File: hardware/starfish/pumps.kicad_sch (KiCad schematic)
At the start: 7 parts, among them J1001 Pump, Q1001 PSMN011-30YLC

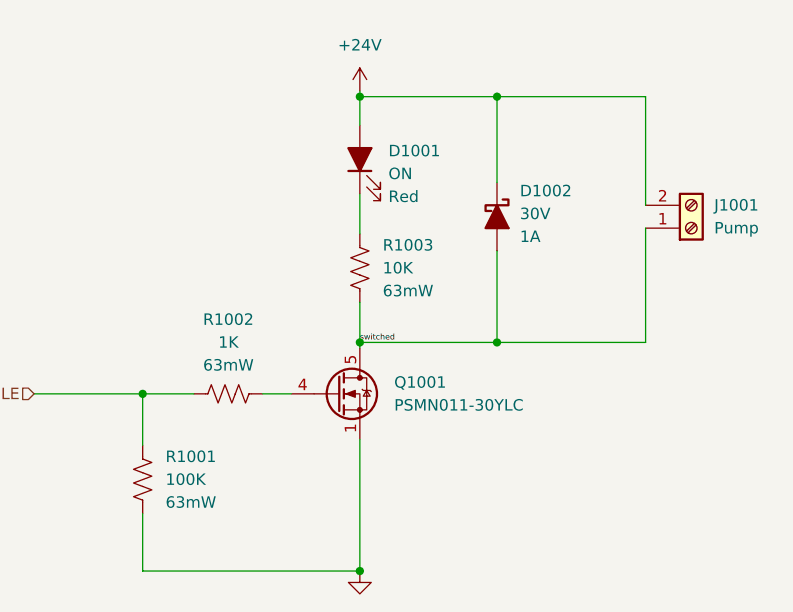
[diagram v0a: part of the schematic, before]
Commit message: Mostly finished starfish schematic, ready for layout!
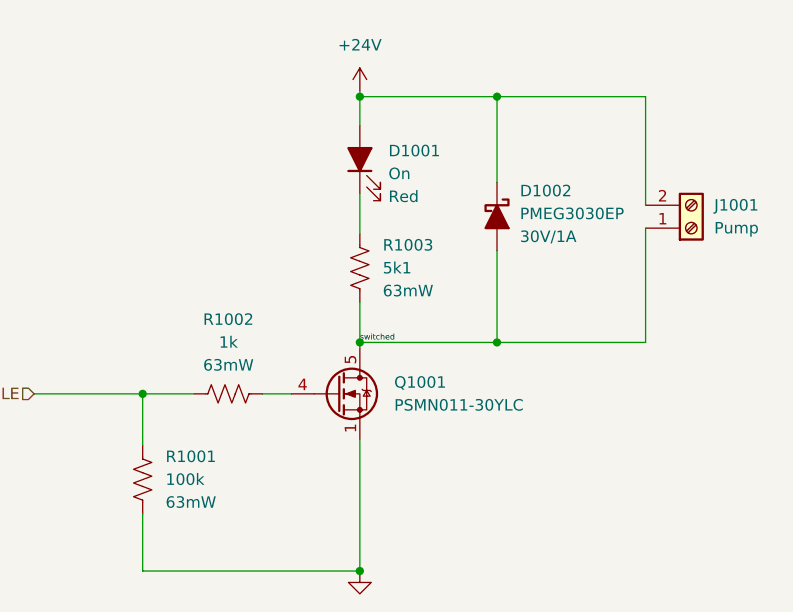
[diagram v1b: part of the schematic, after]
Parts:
- D1001: value ON -> On
- D1002: value 30V -> PMEG3030EP; Rating 1A -> 30V/1A
- Q1001: mpn (none) -> PSMN011-30YLC
- R1001: value 100K -> 100k; footprint (none) -> winterbloom:R_0402_HandSolder
- R1002: value 1K -> 1k; footprint (none) -> winterbloom:R_0402_HandSolder; mpn (none) -> RC0402JR-071KL
- R1003: value 10K -> 5k1; footprint (none) -> winterbloom:R_0402_HandSolder; mpn (none) -> AC0603FR-075K1L
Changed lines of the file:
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@@
       (effects (font (size 1.27 1.27)) (justify right))
     )
-    (property "Value" "ON" (id 1) (at 133.985 75.8824 90)
+    (property "Value" "On" (id 1) (at 133.985 75.8824 90)
       (effects (font (size 1.27 1.27)) (justify right))
     )
@@
       (effects (font (size 1.27 1.27)) (justify left))
     )
-    (property "Value" "100K" (id 1) (at 109.22 109.8549 0)
+    (property "Value" "100k" (id 1) (at 109.22 109.8549 0)
       (effects (font (size 1.27 1.27)) (justify left))
     )
-    (property "Footprint" "" (id 2) (at 107.696 110.109 90)
+    (property "Footprint" "winterbloom:R_0402_HandSolder" (id 2) (at 107.696 110.109 90)
       (effects (font (size 1.27 1.27)) hide)
     )
@@
       (effects (font (size 1.27 1.27)) (justify left))
     )
-    (property "Value" "30V" (id 1) (at 148.59 80.3274 90)
+    (property "Value" "PMEG3030EP" (id 1) (at 148.59 80.3274 90)
       (effects (font (size 1.27 1.27)) (justify left))
     )
@@
       (effects (font (size 1.27 1.27)) hide)
     )
-    (property "Rating" "1A" (id 4) (at 148.59 82.8674 90)
+    (property "Rating" "30V/1A" (id 4) (at 148.59 82.8674 90)
       (effects (font (size 1.27 1.27)) (justify left))
     )
@@
     (in_bom yes) (on_board yes) (fields_autoplaced)
     (property "Reference" "R1002" (id 0) (at 116.205 92.075 90))
-    (property "Value" "1K" (id 1) (at 116.205 94.615 90))
-    (property "Footprint" "" (id 2) (at 116.459 99.314 90)
+    (property "Value" "1k" (id 1) (at 116.205 94.615 90))
+    (property "Footprint" "winterbloom:R_0402_HandSolder" (id 2) (at 116.459 99.314 90)
       (effects (font (size 1.27 1.27)) hide)
     )
@@
     )
     (property "Rating" "63mW" (id 4) (at 116.205 97.155 90))
+    (property "mpn" "RC0402JR-071KL" (id 5) (at 116.205 100.33 0)
+      (effects (font (size 1.27 1.27)) hide)
+    )
     (pin "1")
     (pin "2")
@@
       (effects (font (size 1.27 1.27)) (justify left))
     )
-    (property "Value" "10K" (id 1) (at 133.35 86.3599 0)
+    (property "Value" "5k1" (id 1) (at 133.35 86.3599 0)
       (effects (font (size 1.27 1.27)) (justify left))
     )
-    (property "Footprint" "" (id 2) (at 131.826 86.614 90)
+    (property "Footprint" "winterbloom:R_0402_HandSolder" (id 2) (at 131.826 86.614 90)
       (effects (font (size 1.27 1.27)) hide)
     )
@@
       (effects (font (size 1.27 1.27)) hide)
     )
-    (property "mpn" "" (id 4) (at 130.81 86.36 0)
+    (property "mpn" "AC0603FR-075K1L" (id 4) (at 130.81 86.36 0)
       (effects (font (size 1.27 1.27)) hide)
     )
@@
       (effects (font (size 1.27 1.27)) hide)
     )
+    (property "mpn" "PSMN011-30YLC" (id 4) (at 128.27 100.33 0)
+      (effects (font (size 1.27 1.27)) hide)
+    )

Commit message: Layout and routing mostly done! Just gotta make it prettier!
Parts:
- D1002: footprint Diode_SMD:D_SOD-128 -> winterbloom:D_SOD-128
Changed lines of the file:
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@@
       (effects (font (size 1.27 1.27)) (justify left))
     )
-    (property "Footprint" "Diode_SMD:D_SOD-128" (id 2) (at 146.05 80.645 0)
+    (property "Footprint" "winterbloom:D_SOD-128" (id 2) (at 146.05 80.645 0)
       (effects (font (size 1.27 1.27)) hide)
     )

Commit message: Run through purchasing, update some cap sizes
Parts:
- D1002: mpn (none) -> PMEG3030EP,115
- Q1001: mpn PSMN011-30YLC -> PSMN011-30YLC, BUK9Y40-55B
- R1001: mpn (none) -> RC0402DR-07100KL
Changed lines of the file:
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@@
       (effects (font (size 1.27 1.27)) (justify left))
+    )
+    (property "mpn" "RC0402DR-07100KL" (id 5) (at 106.68 109.855 0)
+      (effects (font (size 1.27 1.27)) hide)
     )
     (pin "1")
@@
     (property "Rating" "30V/1A" (id 4) (at 148.59 82.8674 90)
       (effects (font (size 1.27 1.27)) (justify left))
+    )
+    (property "mpn" "PMEG3030EP,115" (id 5) (at 146.05 80.645 0)
+      (effects (font (size 1.27 1.27)) hide)
     )
     (pin "1")
@@
       (effects (font (size 1.27 1.27)) hide)
     )
-    (property "mpn" "PSMN011-30YLC" (id 4) (at 128.27 100.33 0)
+    (property "mpn" "PSMN011-30YLC, BUK9Y40-55B" (id 4) (at 128.27 100.33 0)
       (effects (font (size 1.27 1.27)) hide)
     )
